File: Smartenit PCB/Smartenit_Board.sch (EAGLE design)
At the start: 91 parts, among them J1 2X5CONNECTOR1.27MM, U1 SN74LVC1G3157, U2 ADE7953, U3 ESP-WROOM-32

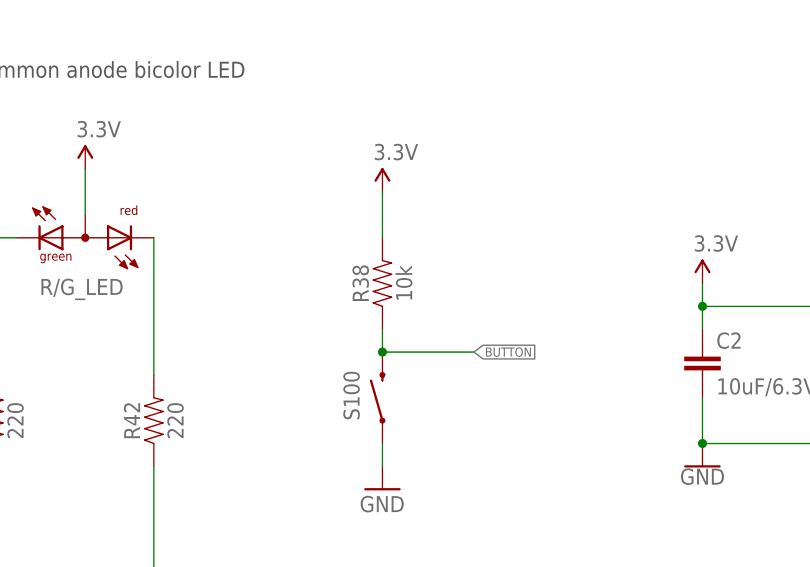
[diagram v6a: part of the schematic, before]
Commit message: changes to brandy_testeeprom and pull down
changed pull down on button to 4.7.
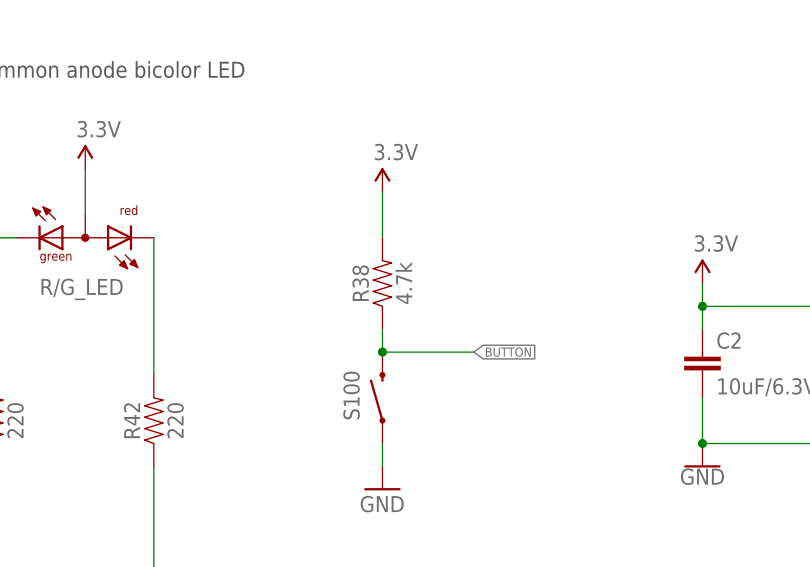
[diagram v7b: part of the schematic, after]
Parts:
- R38: value 10k -> 4.7k
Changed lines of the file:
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@@
 <grid distance="0.1" unitdist="inch" unit="inch" style="lines" multiple="1" display="no" altdistance="0.01" altunitdist="inch" altunit="inch"/>
 <layers>
-<layer number="1" name="Top" color="4" fill="1" visible="no" active="no"/>
-<layer number="2" name="Route2" color="1" fill="3" visible="no" active="no"/>
-<layer number="3" name="Route3" color="4" fill="3" visible="no" active="no"/>
-<layer number="4" name="Route4" color="1" fill="4" visible="no" active="no"/>
-<layer number="5" name="Route5" color="4" fill="4" visible="no" active="no"/>
-<layer number="6" name="Route6" color="1" fill="8" visible="no" active="no"/>
-<layer number="7" name="Route7" color="4" fill="8" visible="no" active="no"/>
-<layer number="8" name="Route8" color="1" fill="2" visible="no" active="no"/>
-<layer number="9" name="Route9" color="4" fill="2" visible="no" active="no"/>
-<layer number="10" name="Route10" color="1" fill="7" visible="no" active="no"/>
-<layer number="11" name="Route11" color="4" fill="7" visible="no" active="no"/>
-<layer number="12" name="Route12" color="1" fill="5" visible="no" active="no"/>
-<layer number="13" name="Route13" color="4" fill="5" visible="no" active="no"/>
-<layer number="14" name="Route14" color="1" fill="6" visible="no" active="no"/>
-<layer number="15" name="Route15" color="4" fill="6" visible="no" active="no"/>
-<layer number="16" name="Bottom" color="1" fill="1" visible="no" active="no"/>
-<layer number="17" name="Pads" color="2" fill="1" visible="no" active="no"/>
-<layer number="18" name="Vias" color="2" fill="1" visible="no" active="no"/>
-<layer number="19" name="Unrouted" color="6" fill="1" visible="no" active="no"/>
-<layer number="20" name="Dimension" color="15" fill="1" visible="no" active="no"/>
-<layer number="21" name="tPlace" color="7" fill="1" visible="no" active="no"/>
-<layer number="22" name="bPlace" color="7" fill="1" visible="no" active="no"/>
-<layer number="23" name="tOrigins" color="15" fill="1" visible="no" active="no"/>
-<layer number="24" name="bOrigins" color="15" fill="1" visible="no" active="no"/>
-<layer number="25" name="tNames" color="7" fill="1" visible="no" active="no"/>
-<layer number="26" name="bNames" color="7" fill="1" visible="no" active="no"/>
-<layer number="27" name="tValues" color="7" fill="1" visible="no" active="no"/>
-<layer number="28" name="bValues" color="7" fill="1" visible="no" active="no"/>
+<layer number="1" name="Top" color="4" fill="1" visible="yes" active="no"/>
+<layer number="2" name="Route2" color="1" fill="3" visible="yes" active="no"/>
+<layer number="3" name="Route3" color="4" fill="3" visible="yes" active="no"/>
+<layer number="4" name="Route4" color="1" fill="4" visible="yes" active="no"/>
+<layer number="5" name="Route5" color="4" fill="4" visible="yes" active="no"/>
+<layer number="6" name="Route6" color="1" fill="8" visible="yes" active="no"/>
+<layer number="7" name="Route7" color="4" fill="8" visible="yes" active="no"/>
+<layer number="8" name="Route8" color="1" fill="2" visible="yes" active="no"/>
+<layer number="9" name="Route9" color="4" fill="2" visible="yes" active="no"/>
+<layer number="10" name="Route10" color="1" fill="7" visible="yes" active="no"/>
+<layer number="11" name="Route11" color="4" fill="7" visible="yes" active="no"/>
+<layer number="12" name="Route12" color="1" fill="5" visible="yes" active="no"/>
+<layer number="13" name="Route13" color="4" fill="5" visible="yes" active="no"/>
+<layer number="14" name="Route14" color="1" fill="6" visible="yes" active="no"/>
+<layer number="15" name="Route15" color="4" fill="6" visible="yes" active="no"/>
+<layer number="16" name="Bottom" color="1" fill="1" visible="yes" active="no"/>
+<layer number="17" name="Pads" color="2" fill="1" visible="yes" active="no"/>
+<layer number="18" name="Vias" color="2" fill="1" visible="yes" active="no"/>
+<layer number="19" name="Unrouted" color="6" fill="1" visible="yes" active="no"/>
+<layer number="20" name="Dimension" color="15" fill="1" visible="yes" active="no"/>
+<layer number="21" name="tPlace" color="7" fill="1" visible="yes" active="no"/>
+<layer number="22" name="bPlace" color="7" fill="1" visible="yes" active="no"/>
+<layer number="23" name="tOrigins" color="15" fill="1" visible="yes" active="no"/>
+<layer number="24" name="bOrigins" color="15" fill="1" visible="yes" active="no"/>
+<layer number="25" name="tNames" color="7" fill="1" visible="yes" active="no"/>
+<layer number="26" name="bNames" color="7" fill="1" visible="yes" active="no"/>
+<layer number="27" name="tValues" color="7" fill="1" visible="yes" active="no"/>
+<layer number="28" name="bValues" color="7" fill="1" visible="yes" active="no"/>
 <layer number="29" name="tStop" color="7" fill="3" visible="no" active="no"/>
 <layer number="30" name="bStop" color="7" fill="6" visible="no" active="no"/>
@@
 <layer number="35" name="tGlue" color="7" fill="4" visible="no" active="no"/>
 <layer number="36" name="bGlue" color="7" fill="5" visible="no" active="no"/>
-<layer number="37" name="tTest" color="7" fill="1" visible="no" active="no"/>
-<layer number="38" name="bTest" color="7" fill="1" visible="no" active="no"/>
+<layer number="37" name="tTest" color="7" fill="1" visible="yes" active="no"/>
+<layer number="38" name="bTest" color="7" fill="1" visible="yes" active="no"/>
 <layer number="39" name="tKeepout" color="4" fill="11" visible="no" active="no"/>
 <layer number="40" name="bKeepout" color="1" fill="11" visible="no" active="no"/>
@@
 <layer number="44" name="Drills" color="7" fill="1" visible="no" active="no"/>
 <layer number="45" name="Holes" color="7" fill="1" visible="no" active="no"/>
-<layer number="46" name="Milling" color="3" fill="1" visible="no" active="no"/>
-<layer number="47" name="Measures" color="7" fill="1" visible="no" active="no"/>
-<layer number="48" name="Document" color="7" fill="1" visible="no" active="no"/>
-<layer number="49" name="Reference" color="14" fill="1" visible="no" active="no"/>
-<layer number="50" name="dxf" color="7" fill="1" visible="no" active="no"/>
-<layer number="51" name="tDocu" color="6" fill="1" visible="no" active="no"/>
-<layer number="52" name="bDocu" color="6" fill="1" visible="no" active="no"/>
-<layer number="53" name="tGND_GNDA" color="7" fill="9" visible="no" active="no"/>
-<layer number="54" name="bGND_GNDA" color="1" fill="9" visible="no" active="no"/>
-<layer number="56" name="wert" color="7" fill="1" visible="no" active="no"/>
-<layer number="57" name="tCAD" color="7" fill="1" visible="no" active="no"/>
-<layer number="59" name="tCarbon" color="7" fill="1" visible="no" active="no"/>
-<layer number="60" name="bCarbon" color="7" fill="1" visible="no" active="no"/>
+<layer number="46" name="Milling" color="3" fill="1" visible="yes" active="no"/>
+<layer number="47" name="Measures" color="7" fill="1" visible="yes" active="no"/>
+<layer number="48" name="Document" color="7" fill="1" visible="yes" active="no"/>
+<layer number="49" name="Reference" color="14" fill="1" visible="yes" active="no"/>
+<layer number="50" name="dxf" color="7" fill="1" visible="yes" active="no"/>
+<layer number="51" name="tDocu" color="6" fill="1" visible="yes" active="no"/>
+<layer number="52" name="bDocu" color="6" fill="1" visible="yes" active="no"/>
+<layer number="53" name="tGND_GNDA" color="7" fill="9" visible="yes" active="no"/>
+<layer number="54" name="bGND_GNDA" color="1" fill="9" visible="yes" active="no"/>
+<layer number="56" name="wert" color="7" fill="1" visible="yes" active="no"/>
+<layer number="57" name="tCAD" color="7" fill="1" visible="yes" active="no"/>
+<layer number="59" name="tCarbon" color="7" fill="1" visible="yes" active="no"/>
+<layer number="60" name="bCarbon" color="7" fill="1" visible="yes" active="no"/>
 <layer number="88" name="SimResults" color="9" fill="1" visible="no" active="yes"/>
 <layer number="89" name="SimProbes" color="9" fill="1" visible="no" active="yes"/>
@@
 <part name="P+4" library="SparkFun" deviceset="3.3V" device=""/>
 <part name="P+1" library="SparkFun" deviceset="3.3V" device=""/>
-<part name="R38" library="SparkFun-Resistors" deviceset="10KOHM" device="-0603-1/10W-1%" value="10k"/>
+<part name="R38" library="SparkFun-Resistors" deviceset="10KOHM" device="-0603-1/10W-1%" value="4.7k"/>
 <part name="R33" library="SparkFun-Resistors" deviceset="10KOHM" device="-0603-1/10W-1%" value="220"/>
 <part name="R41" library="SparkFun-Resistors" deviceset="10KOHM" device="-0603-1/10W-1%" value="220"/>
